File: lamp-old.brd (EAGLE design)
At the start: 127 x 38.1 mm, 54 parts

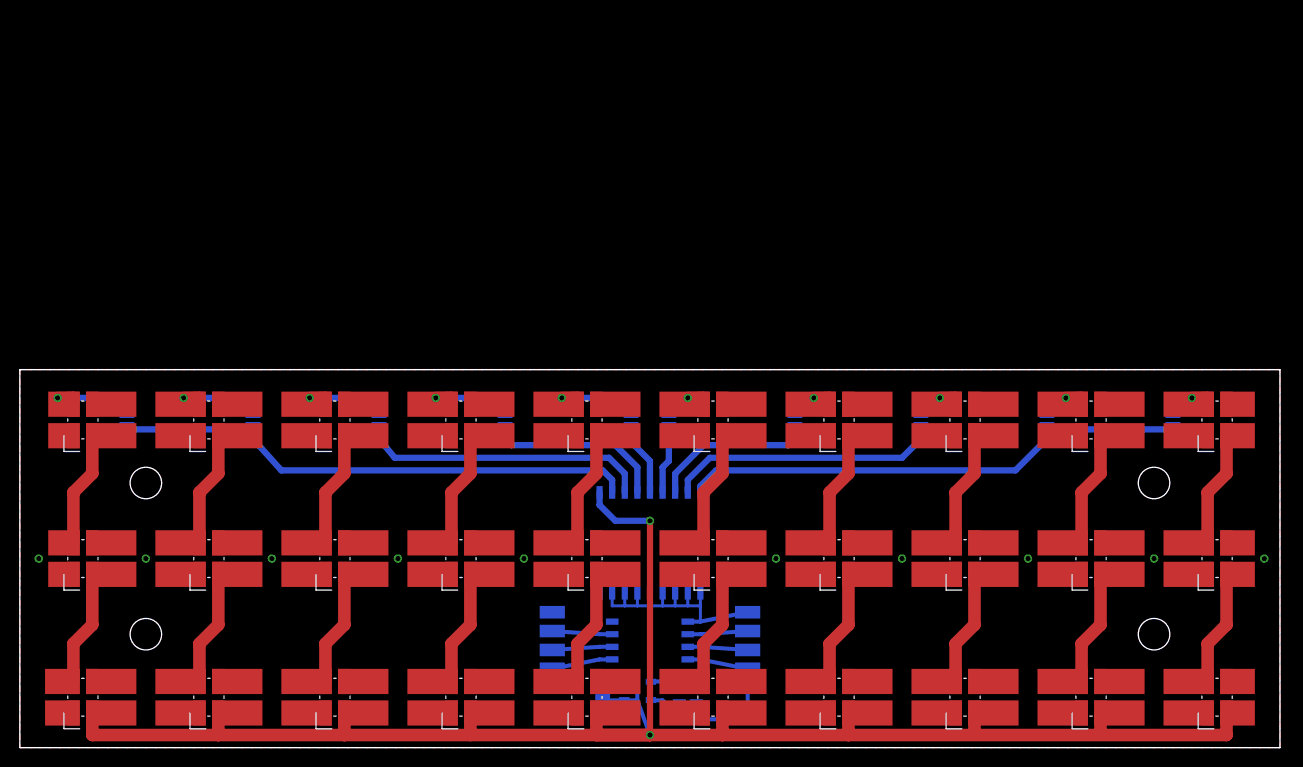
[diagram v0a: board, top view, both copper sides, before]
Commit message: More fiddling: moved some parts around, started adding capacitive touch on/off switch
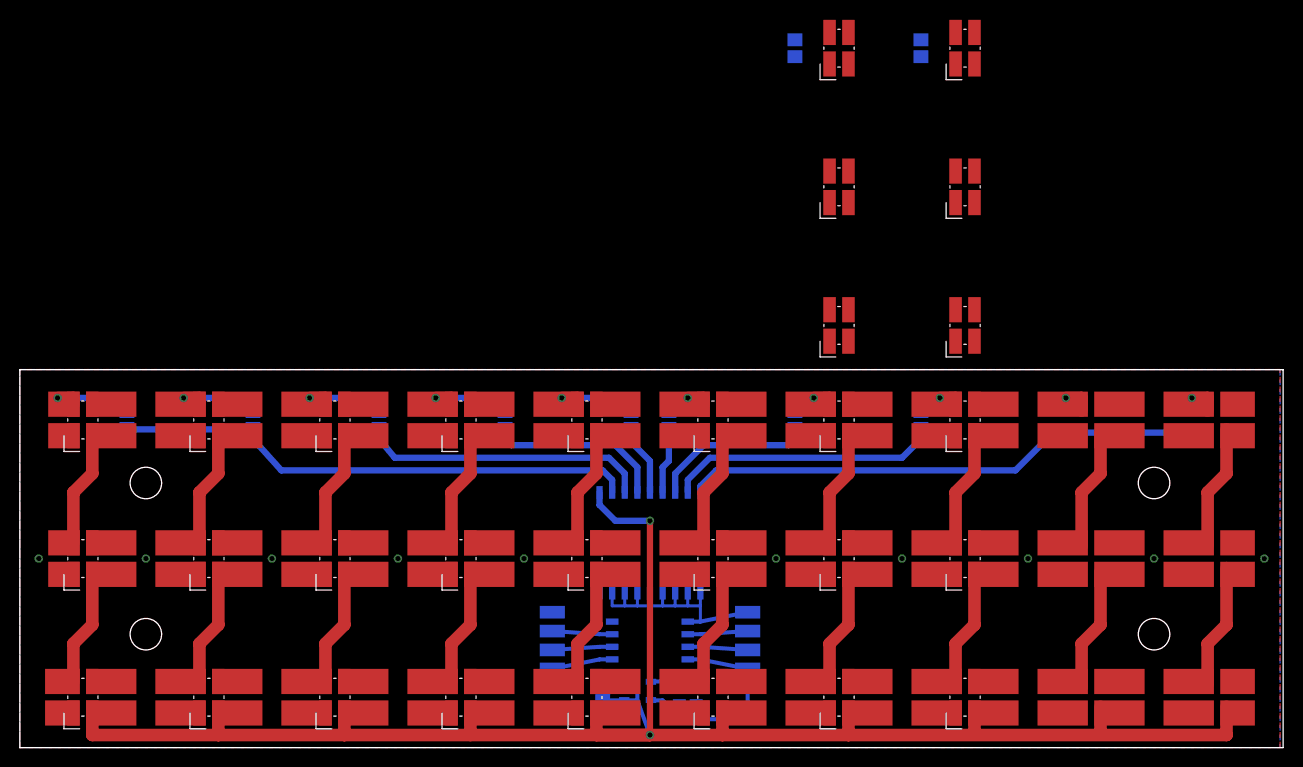
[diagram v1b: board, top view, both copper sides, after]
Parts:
- moved U$2 53.4 mm to (82.5, 42.5)
- moved U$3 53.4 mm to (82.5, 56.5)
- moved U$4 53.4 mm to (82.5, 70.5)
- moved R1 53.4 mm to (78.1, 70.5)
- moved U$5 39.6 mm to (95.2, 42.5)
- moved U$6 39.6 mm to (95.2, 56.5)
- moved U$7 39.6 mm to (95.2, 70.5)
- moved R2 39.6 mm to (90.8, 70.5)
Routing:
- net N$50: track 0.00 -> 12.5 mm
- net N$53: track 0.00 -> 12.5 mm
- net N$49: track 0.00 -> 12.5 mm
- net N$54: track 0.00 -> 12.2 mm
- net N$6: track 11.6 -> 0.00 mm
- net N$3: track 11.6 -> 0.00 mm
- net N$4: track 11.6 -> 0.00 mm
- net N$1: track 11.6 -> 0.00 mm
- net N$51: track 0.00 -> 5.29 mm, vias 0 -> 1
- net N$45: track 0.00 -> 5.29 mm, vias 0 -> 1
- net N$2: track 4.65 -> 0.00 mm, vias 1 -> 0
- net N$5: track 4.65 -> 0.00 mm, vias 1 -> 0
- net +12V: track 178.0 -> 179.3 mm
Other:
- board size 127 x 38.1 mm -> 127.3 x 38.1 mm
